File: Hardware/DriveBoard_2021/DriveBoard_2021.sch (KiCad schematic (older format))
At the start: 89 parts, among them SW1 SW_Push, SW2 SW_Push, SW3 SW_Push, SW4 SW_Push, SW5 SW_Push, SW6 SW_Push, SW7 SW_Push, U1 LM2576S-3.3, U2 LM2576HVS-5, U3 TM4C129E_Launchpad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

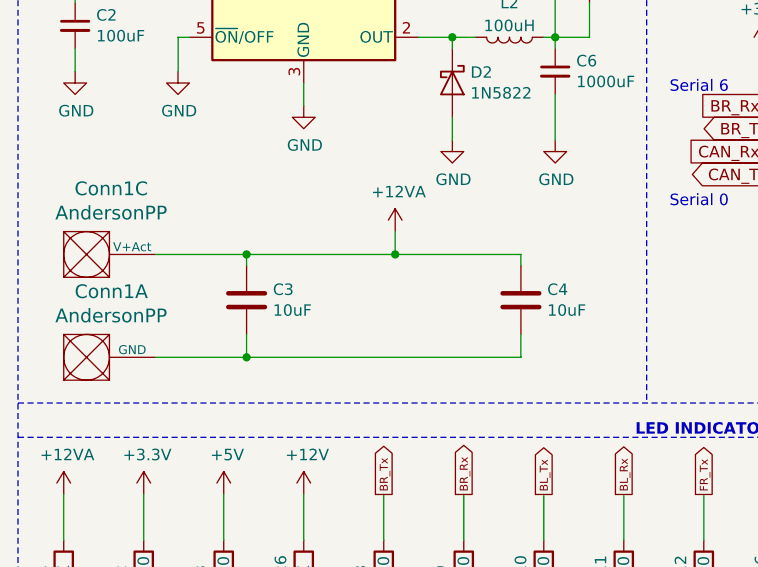
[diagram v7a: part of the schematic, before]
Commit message: All Components in Place. Small amounts of trace work remaining.
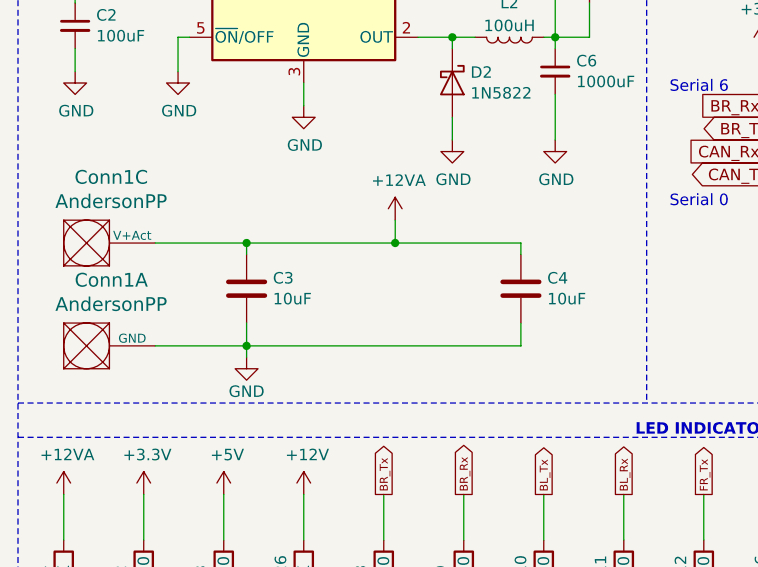
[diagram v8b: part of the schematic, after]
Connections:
- net GND: now also C3.2, C4.2, Conn1.1 (GND)
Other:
- moved on the sheet: C3, C4, Conn1A, Conn1C
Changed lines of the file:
@@
 L MRDT_Connectors:AndersonPP Conn1
 U 1 1 5F626395
-P 700 3800
-F 0 "Conn1" H 908 4187 60  0000 C CNN
-F 1 "AndersonPP" H 908 4081 60  0000 C CNN
-F 2 "MRDT_Connectors:Anderson_3_Horizontal_Side_by_Side" H 550 3250 60  0001 C CNN
-F 3 "" H 550 3250 60  0001 C CNN
-	1    700  3800
+P 700 3750
+F 0 "Conn1" H 908 4137 60  0000 C CNN
+F 1 "AndersonPP" H 908 4031 60  0000 C CNN
+F 2 "MRDT_Connectors:Anderson_3_Horizontal_Side_by_Side" H 550 3200 60  0001 C CNN
+F 3 "" H 550 3200 60  0001 C CNN
+	1    700  3750
 	1    0    0    -1
 $EndComp
@@
 L Device:C C3
 U 1 1 5F64B4C7
-P 1500 3450
-F 0 "C3" H 1615 3496 50  0000 L CNN
-F 1 "10uF" H 1615 3405 50  0000 L CNN
-F 2 "Capacitor_SMD:C_0603_1608Metric_Pad1.05x0.95mm_HandSolder" H 1538 3300 50  0001 C CNN
-F 3 "~" H 1500 3450 50  0001 C CNN
-	1    1500 3450
+P 1500 3400
+F 0 "C3" H 1615 3446 50  0000 L CNN
+F 1 "10uF" H 1615 3355 50  0000 L CNN
+F 2 "Capacitor_SMD:C_0603_1608Metric_Pad1.05x0.95mm_HandSolder" H 1538 3250 50  0001 C CNN
+F 3 "~" H 1500 3400 50  0001 C CNN
+	1    1500 3400
 	1    0    0    -1
 $EndComp
@@
 L Device:C C4
 U 1 1 5F64B4CD
-P 2700 3450
-F 0 "C4" H 2815 3496 50  0000 L CNN
-F 1 "10uF" H 2815 3405 50  0000 L CNN
-F 2 "Capacitor_SMD:C_0603_1608Metric_Pad1.05x0.95mm_HandSolder" H 2738 3300 50  0001 C CNN
-F 3 "~" H 2700 3450 50  0001 C CNN
-	1    2700 3450
-	1    0    0    -1
-$EndComp
-Wire Wire Line
-	1500 3300 1500 3250
-Wire Wire Line
-	2700 3300 2700 3250
-Wire Wire Line
-	2700 3600 2700 3700
-Wire Wire Line
-	1500 3250 2150 3250
+P 2700 3400
+F 0 "C4" H 2815 3446 50  0000 L CNN
+F 1 "10uF" H 2815 3355 50  0000 L CNN
+F 2 "Capacitor_SMD:C_0603_1608Metric_Pad1.05x0.95mm_HandSolder" H 2738 3250 50  0001 C CNN
+F 3 "~" H 2700 3400 50  0001 C CNN
+	1    2700 3400
+	1    0    0    -1
+$EndComp
+Wire Wire Line
+	1500 3250 1500 3200
+Wire Wire Line
+	2700 3250 2700 3200
+Wire Wire Line
+	2700 3550 2700 3650
+Wire Wire Line
+	1500 3200 2150 3200
 $Comp
 L power:+12VA #PWR020
 U 1 1 5F651487
-P 2150 3150
-F 0 "#PWR020" H 2150 3000 50  0001 C CNN
-F 1 "+12VA" H 2165 3323 50  0000 C CNN
-F 2 "" H 2150 3150 50  0001 C CNN
-F 3 "" H 2150 3150 50  0001 C CNN
-	1    2150 3150
+P 2150 3100
+F 0 "#PWR020" H 2150 2950 50  0001 C CNN
+F 1 "+12VA" H 2165 3273 50  0000 C CNN
+F 2 "" H 2150 3100 50  0001 C CNN
+F 3 "" H 2150 3100 50  0001 C CNN
+	1    2150 3100
 	1    0    0    -1
 $EndComp
@@
 	3000 1200 3000 1050
 Wire Wire Line
-	1100 3700 1500 3700
-Wire Wire Line
-	1500 3600 1500 3700
-Connection ~ 1500 3700
-Wire Wire Line
-	1500 3700 2700 3700
+	1500 3550 1500 3650
+Connection ~ 1500 3650
+Wire Wire Line
+	1500 3650 2700 3650
 $Comp
 L power:GND #PWR048
@@
 	6000 1300 5900 1300
 Wire Wire Line
-	2150 3150 2150 3250
-Connection ~ 2150 3250
-Wire Wire Line
-	2150 3250 2700 3250
+	2150 3100 2150 3200
+Connection ~ 2150 3200
+Wire Wire Line
+	2150 3200 2700 3200
 Text Notes 1600 600  0    50   ~ 10
 POWER\n
@@
 Wire Wire Line
 	7650 5650 7700 5650
-Connection ~ 1500 3250
-Wire Wire Line
-	1100 3250 1500 3250
+Connection ~ 1500 3200
+Wire Wire Line
+	1100 3200 1500 3200
 $Comp
 L MRDT_Connectors:AndersonPP Conn1
 U 3 1 5F623BE1
-P 700 3350
-F 0 "Conn1" H 908 3737 60  0000 C CNN
-F 1 "AndersonPP" H 908 3631 60  0000 C CNN
-F 2 "MRDT_Connectors:Anderson_3_Horizontal_Side_by_Side" H 550 2800 60  0001 C CNN
-F 3 "" H 550 2800 60  0001 C CNN
-	3    700  3350
+P 700 3300
+F 0 "Conn1" H 908 3687 60  0000 C CNN
+F 1 "AndersonPP" H 908 3581 60  0000 C CNN
+F 2 "MRDT_Connectors:Anderson_3_Horizontal_Side_by_Side" H 550 2750 60  0001 C CNN
+F 3 "" H 550 2750 60  0001 C CNN
+	3    700  3300
 	1    0    0    -1
 $EndComp
@@
 	1    0    0    -1
 $EndComp
+$Comp
+L power:GND #PWR?
+U 1 1 5FB2C97B
+P 1500 3700
+F 0 "#PWR?" H 1500 3450 50  0001 C CNN
+F 1 "GND" H 1500 3550 50  0000 C CNN
+F 2 "" H 1500 3700 50  0001 C CNN
+F 3 "" H 1500 3700 50  0001 C CNN
+	1    1500 3700
+	1    0    0    -1
+$EndComp
+Wire Wire Line
+	1100 3650 1500 3650
+Wire Wire Line
+	1500 3700 1500 3650
 $EndSCHEMATC
